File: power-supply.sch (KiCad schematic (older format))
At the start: 36 parts, among them U3 LMR16030, U4 LMR16030, U7 LM317_TO-252

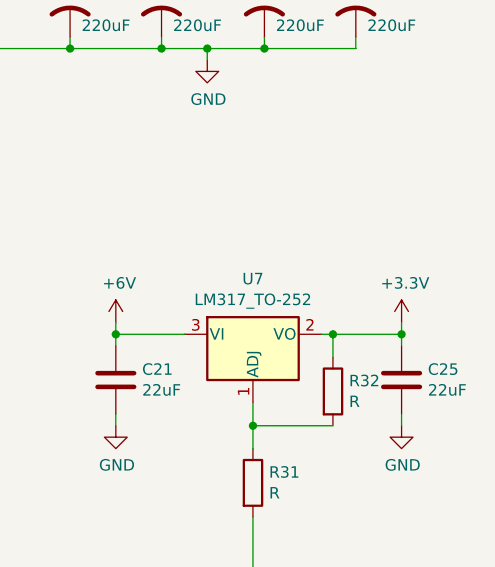
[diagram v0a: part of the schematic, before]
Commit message: Updated JLC and DigiKey parts
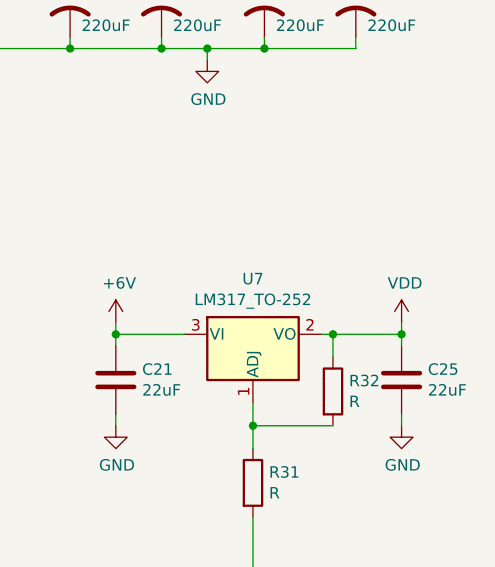
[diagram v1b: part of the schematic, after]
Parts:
- 12V_In_1: footprint Connector_JST:JST_XH_B2B-XH-A_1x02_P2.50mm_Vertical -> Connector_JST:JST_PH_B2B-PH-K_1x02_P2.00mm_Vertical; DigiKey (none) -> 455-1704-ND
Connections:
- net +3V3 renamed VDD
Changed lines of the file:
@@
 $EndComp
 $Comp
-L trap-pcb-rescue:+3.3V-power #PWR0162
+L power:VDD #PWR0162
 U 1 1 5F79D7E5
 P 9850 3400
 F 0 "#PWR0162" H 9850 3250 50  0001 C CNN
-F 1 "+3.3V" H 9865 3573 50  0000 C CNN
+F 1 "VDD" H 9865 3573 50  0000 C CNN
 F 2 "" H 9850 3400 50  0001 C CNN
 F 3 "" H 9850 3400 50  0001 C CNN
@@
 F 0 "12V_In_1" H 7768 1725 50  0000 C CNN
 F 1 "Conn_01x02" H 7768 1816 50  0000 C CNN
-F 2 "Connector_JST:JST_XH_B2B-XH-A_1x02_P2.50mm_Vertical" H 7850 2050 50  0001 C CNN
+F 2 "Connector_JST:JST_PH_B2B-PH-K_1x02_P2.00mm_Vertical" H 7850 2050 50  0001 C CNN
 F 3 "~" H 7850 2050 50  0001 C CNN
+F 4 "455-1704-ND" H 7850 2050 50  0001 C CNN "DigiKey"
 	1    7850 2050
 	-1   0    0    1
